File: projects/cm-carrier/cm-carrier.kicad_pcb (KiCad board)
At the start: 2 copper layers, 0 parts

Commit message: cm-carrier: PCB first pass (sync from schematic, 130x90 outline, block placement, DRC report)
Co-Authored-By: Claude Opus 5.5 <noreply@anthropic.com>
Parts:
- added C1: 10uF 25V, Capacitor_SMD:C_1210_3225Metric, F.Cu at (118.0, 121.0)
- added C10: 100nF, Capacitor_SMD:C_0402_1005Metric, F.Cu at (225.0, 157.0)
- added C11: 100nF, Capacitor_SMD:C_0402_1005Metric, F.Cu at (225.0, 160.0)
- added C12: 100nF, Capacitor_SMD:C_0402_1005Metric, F.Cu at (225.0, 163.0)
- added C13: 10uF 10V, Capacitor_SMD:C_0805_2012Metric, F.Cu at (211.0, 167.0)
- added C14: 10uF 10V, Capacitor_SMD:C_0805_2012Metric, F.Cu at (225.0, 167.0)
- added C15: 1uF 10V, Capacitor_SMD:C_0402_1005Metric, F.Cu at (213.0, 177.0)
- added C16: 1uF 10V, Capacitor_SMD:C_0402_1005Metric, F.Cu at (218.0, 177.0)
- added C17: 1uF 10V, Capacitor_SMD:C_0402_1005Metric, F.Cu at (223.0, 177.0)
- added C18: 10uF 10V, Capacitor_SMD:C_0805_2012Metric, F.Cu at (213.0, 180.5)
- added C19: 10uF 10V, Capacitor_SMD:C_0805_2012Metric, F.Cu at (218.0, 180.5)
- added C2: 100nF, Capacitor_SMD:C_0402_1005Metric, F.Cu at (121.0, 124.5)
- added C20: 10uF 10V, Capacitor_SMD:C_0805_2012Metric, F.Cu at (223.0, 180.5)
- added C21: 470uF, Capacitor_SMD:CP_Elec_8x10, F.Cu at (160.0, 158.0)
- added C22: 100nF, Capacitor_SMD:C_0402_1005Metric, F.Cu at (168.0, 155.0)
- added C23: 33pF, Capacitor_SMD:C_0402_1005Metric, F.Cu at (168.0, 157.5)
- added C24: 10pF, Capacitor_SMD:C_0402_1005Metric, F.Cu at (168.0, 160.0)
- added C25: 100nF, Capacitor_SMD:C_0402_1005Metric, F.Cu at (190.0, 154.0)
- added C26: 33pF, Capacitor_SMD:C_0402_1005Metric, F.Cu at (186.5, 159.0)
- added C27: 33pF, Capacitor_SMD:C_0402_1005Metric, F.Cu at (186.5, 161.5)
- added C28: 33pF, Capacitor_SMD:C_0402_1005Metric, F.Cu at (186.5, 164.0)
- added C29: 100nF, Capacitor_SMD:C_0402_1005Metric, F.Cu at (150.0, 180.0)
- added C3: 3.3nF, Capacitor_SMD:C_0402_1005Metric, F.Cu at (125.0, 125.0)
- added C30: 100nF, Capacitor_SMD:C_0402_1005Metric, F.Cu at (190.0, 175.5)
- added C31: 10uF, Capacitor_SMD:C_0805_2012Metric, F.Cu at (135.0, 116.0)
- added C4: 22uF 6.3V, Capacitor_SMD:C_0805_2012Metric, F.Cu at (137.0, 121.0)
- added C5: 27pF, Capacitor_SMD:C_0402_1005Metric, F.Cu at (213.5, 150.0)
- added C6: 27pF, Capacitor_SMD:C_0402_1005Metric, F.Cu at (222.5, 150.0)
- added C7: 100nF, Capacitor_SMD:C_0402_1005Metric, F.Cu at (211.0, 157.0)
- added C8: 100nF, Capacitor_SMD:C_0402_1005Metric, F.Cu at (211.0, 160.0)
- added C9: 100nF, Capacitor_SMD:C_0402_1005Metric, F.Cu at (211.0, 163.0)
- added D1: LED_ACT green, LED_SMD:LED_0603_1608Metric, F.Cu at (123.0, 113.0)
- added D2: green, LED_SMD:LED_0603_1608Metric, F.Cu at (183.0, 162.0)
- added H1: MountingHole_3.2mm_M3, MountingHole:MountingHole_3.2mm_M3, F.Cu at (104.0, 104.0)
- added H2: MountingHole_3.2mm_M3, MountingHole:MountingHole_3.2mm_M3, F.Cu at (226.0, 104.0)
- added H3: MountingHole_3.2mm_M3, MountingHole:MountingHole_3.2mm_M3, F.Cu at (104.0, 186.0)
- added H4: MountingHole_3.2mm_M3, MountingHole:MountingHole_3.2mm_M3, F.Cu at (226.0, 186.0)
- added J1: XA_5V_IN, Connector_JST:JST_XA_B08B-XASK-1_1x08_P2.50mm_Vertical, F.Cu at (111.0, 105.0)
- added J2: DEBUG_UART, Connector_PinHeader_2.54mm:PinHeader_1x03_P2.54mm_Vertical, F.Cu at (108.0, 112.0)
- added J3: USB_C_HOST (USB2.0), Connector_USB:USB_C_Receptacle_GCT_USB4105-xx-A_16P_TopMnt_Horizontal, F.Cu at (198.0, 186.3)
- added J4: XA_USB1, Connector_JST:JST_XA_B04B-XASK-1_1x04_P2.50mm_Vertical, F.Cu at (162.0, 105.0)
- added J5: XA_USB2, Connector_JST:JST_XA_B04B-XASK-1_1x04_P2.50mm_Vertical, F.Cu at (177.0, 105.0)
- added J6: EC25-J Mini PCIe, Connector_PCBEdge:BUS_PCI_Express_Mini_Full, F.Cu at (160.0, 135.0)
- added J7: nanoSIM, Connector_Card:nanoSIM_GCT_SIM8060-6-0-14-00, F.Cu at (200.0, 160.0)
- added J8: micro HDMI (Type D), Connector_Video:HDMI_Micro-D_Molex_46765-2xxx, F.Cu at (182.0, 187.6)
- added J9: microSD, Connector_Card:microSD_HC_Hirose_DM3AT-SF-PEJM5, F.Cu at (148.0, 108.9)
- added L1: 2.2uH XFL4020-222MEB, Inductor_SMD:L_Coilcraft_XxL4020, F.Cu at (131.0, 121.0)
- added Module1: CM4/CM5 (Lite), CM5IO:Raspberry-Pi-5-Compute-Module, F.Cu at (110.0, 178.0)
- added Q1: 2N7002, Package_TO_SOT_SMD:SOT-23, F.Cu at (173.0, 156.0)
- added Q2: 2N7002, Package_TO_SOT_SMD:SOT-23, F.Cu at (173.0, 162.0)
- added R1: 100k, Resistor_SMD:R_0402_1005Metric, F.Cu at (121.0, 118.5)
- added R10: 56k, Resistor_SMD:R_0402_1005Metric, F.Cu at (208.0, 178.0)
- added R11: 10k, Resistor_SMD:R_0402_1005Metric, F.Cu at (214.0, 141.5)
- added R12: 10k, Resistor_SMD:R_0402_1005Metric, F.Cu at (217.0, 141.5)
- added R13: 10k, Resistor_SMD:R_0402_1005Metric, F.Cu at (220.0, 141.5)
- added R14: 100k, Resistor_SMD:R_0402_1005Metric, F.Cu at (177.0, 156.0)
- added R15: 100k, Resistor_SMD:R_0402_1005Metric, F.Cu at (177.0, 162.0)
- added R16: 10k, Resistor_SMD:R_0402_1005Metric, F.Cu at (180.0, 156.0)
- added R17: 1k, Resistor_SMD:R_0402_1005Metric, F.Cu at (180.0, 162.0)
- added R18: 15k, Resistor_SMD:R_0402_1005Metric, F.Cu at (190.0, 156.5)
- added R19: 0R, Resistor_SMD:R_0402_1005Metric, F.Cu at (190.0, 159.0)
- added R2: 100k, Resistor_SMD:R_0402_1005Metric, F.Cu at (129.0, 125.5)
- added R20: 0R, Resistor_SMD:R_0402_1005Metric, F.Cu at (190.0, 161.5)
- added R21: 0R, Resistor_SMD:R_0402_1005Metric, F.Cu at (190.0, 164.0)
- added R22: 470R, Resistor_SMD:R_0402_1005Metric, F.Cu at (149.0, 184.0)
- added R23: 470R, Resistor_SMD:R_0402_1005Metric, F.Cu at (151.5, 184.0)
- added R24: 10k 1%, Resistor_SMD:R_0402_1005Metric, F.Cu at (138.5, 116.0)
- added R3: 1k, Resistor_SMD:R_0402_1005Metric, F.Cu at (123.0, 115.5)
- added R4: 12k 1%, Resistor_SMD:R_0402_1005Metric, F.Cu at (214.0, 145.0)
- added R5: 36k 1%, Resistor_SMD:R_0402_1005Metric, F.Cu at (217.0, 145.0)
- added R6: 36k 1%, Resistor_SMD:R_0402_1005Metric, F.Cu at (220.0, 145.0)
- added R7: 36k 1%, Resistor_SMD:R_0402_1005Metric, F.Cu at (223.0, 145.0)
- added R8: 36k 1%, Resistor_SMD:R_0402_1005Metric, F.Cu at (226.0, 145.0)
- added R9: 56k, Resistor_SMD:R_0402_1005Metric, F.Cu at (205.0, 178.0)
- added SW1: PWR_BUT, Button_Switch_SMD:SW_SPST_TL3342, F.Cu at (116.0, 114.0)
- added U1: TPS62132, Package_DFN_QFN:VQFN-16-1EP_3x3mm_P0.5mm_EP1.68x1.68mm_ThermalVias, F.Cu at (125.0, 121.0)
- added U10: TPD4EUSB30, Package_SON:USON-10_2.5x1.0mm_P0.5mm, F.Cu at (150.0, 172.0)
- added U11: TPD4EUSB30, Package_SON:USON-10_2.5x1.0mm_P0.5mm, F.Cu at (150.0, 176.0)
- added U12: MagJack A70-112-331N126, CM5IO:TRJG0926HENL, F.Cu at (163.0, 179.1)
- added U13: TPD4EUSB30, Package_SON:USON-10_2.5x1.0mm_P0.5mm, F.Cu at (178.0, 176.0)
- added U14: TPD4EUSB30, Package_SON:USON-10_2.5x1.0mm_P0.5mm, F.Cu at (182.0, 176.0)
- added U15: TPD4EUSB30, Package_SON:USON-10_2.5x1.0mm_P0.5mm, F.Cu at (186.0, 176.0)
- added U16: RT9742SNGV, Package_TO_SOT_SMD:TSOT-23_HandSoldering, F.Cu at (190.0, 171.0)
- added U17: RT9742GGJ5, Package_TO_SOT_SMD:SOT-23-5, F.Cu at (136.0, 112.0)
- added U2: USB2514B-I/M2, Package_DFN_QFN:QFN-36-1EP_6x6mm_P0.5mm_EP3.7x3.7mm, F.Cu at (218.0, 160.0)
- added U3: TPS2051CDBV, Package_TO_SOT_SMD:SOT-23-5, F.Cu at (213.0, 173.0)
- added U4: TPS2051CDBV, Package_TO_SOT_SMD:SOT-23-5, F.Cu at (218.0, 173.0)
- added U5: TPS2051CDBV, Package_TO_SOT_SMD:SOT-23-5, F.Cu at (223.0, 173.0)
- added U6: USBLC6-2SC6, Package_TO_SOT_SMD:SOT-23-6, F.Cu at (198.0, 178.0)
- added U7: USBLC6-2SC6, Package_TO_SOT_SMD:SOT-23-6, F.Cu at (166.0, 112.0)
- added U8: USBLC6-2SC6, Package_TO_SOT_SMD:SOT-23-6, F.Cu at (181.0, 112.0)
- added U9: TPD4E05U06DQA, Package_SON:USON-10_2.5x1.0mm_P0.5mm, F.Cu at (186.5, 155.0)
- added Y1: 24MHz CL=18pF, Crystal:Crystal_SMD_3225-4Pin_3.2x2.5mm, F.Cu at (218.0, 150.0)
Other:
- board outline added: 130 x 90 mm

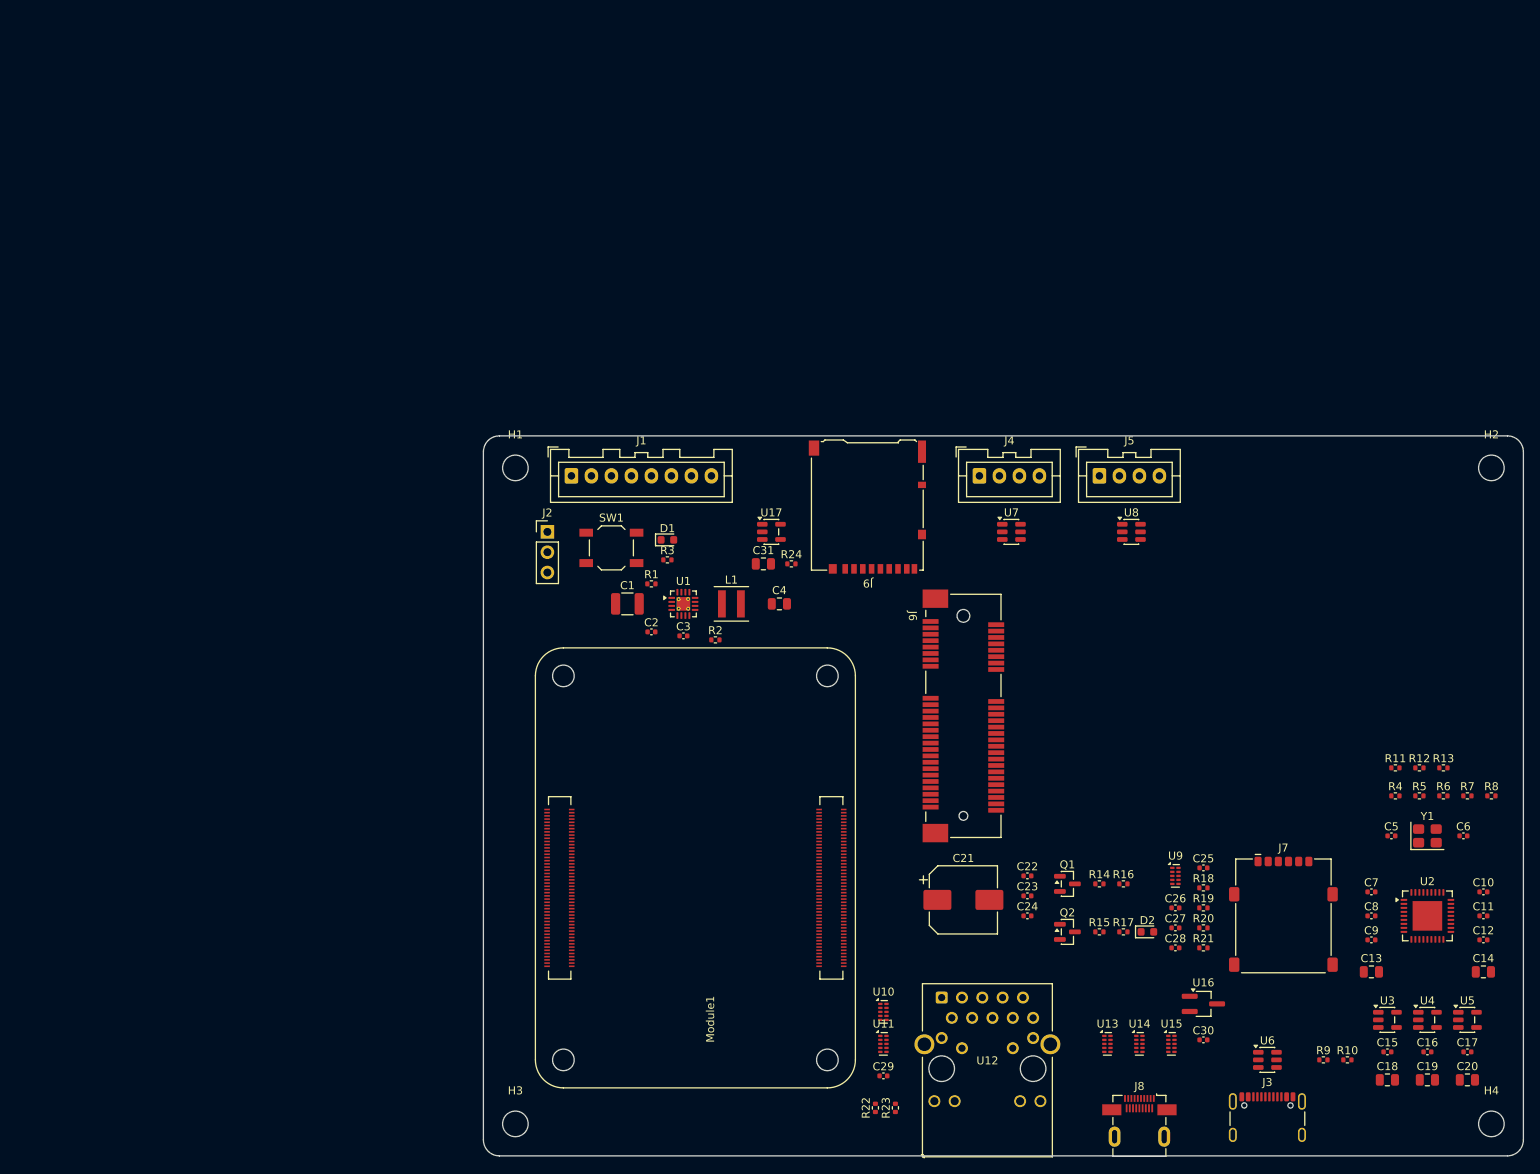
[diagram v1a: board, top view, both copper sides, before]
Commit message: cm-carrier: snapshot GUI-saved board before re-applying JLCPCB rules
Co-Authored-By: Claude Opus 5.5 <noreply@anthropic.com>
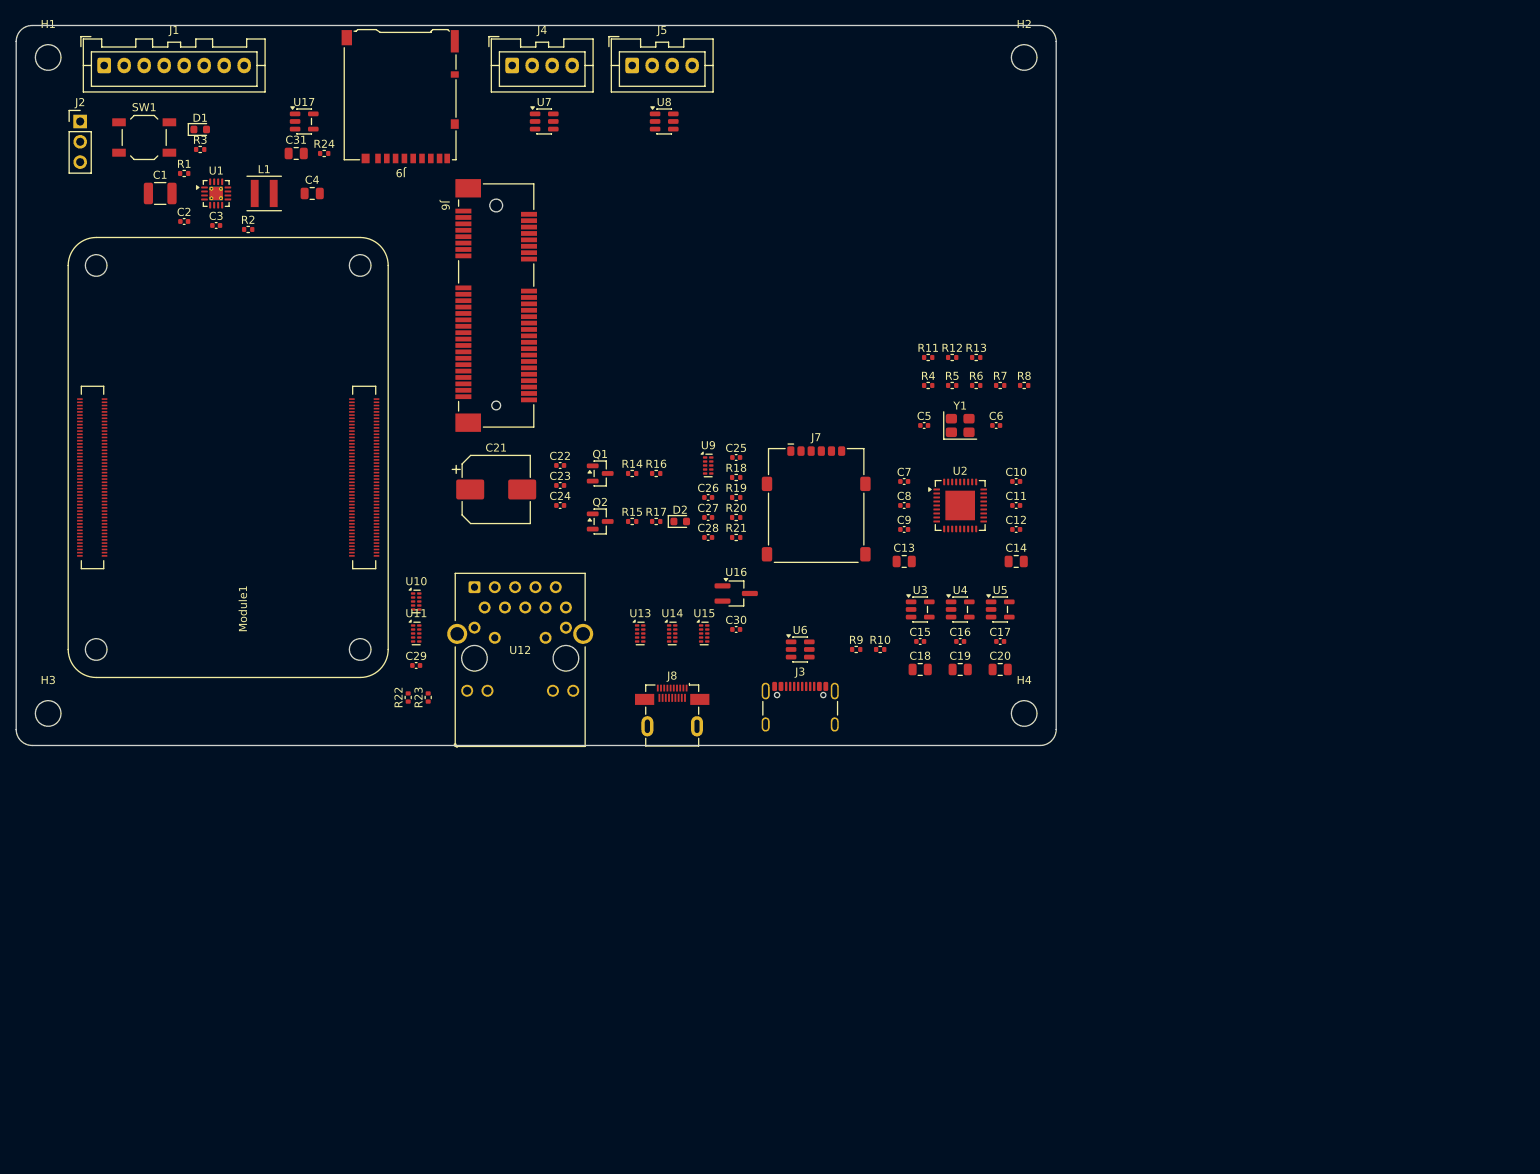
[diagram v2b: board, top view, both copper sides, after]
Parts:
- moved C18 77.7 mm to (154.6, 129.2)
- moved C19 77.7 mm to (159.6, 129.2)
- moved C20 77.7 mm to (164.6, 129.2)
- moved C29 77.7 mm to (91.6, 128.7)
- moved H4 77.7 mm to (167.6, 134.7)
- moved J3 77.7 mm to (139.6, 135.0)
- moved R22 77.7 mm to (90.6, 132.7)
- moved R23 77.7 mm to (93.1, 132.7)
- moved C10 77.7 mm to (166.6, 105.7)
- moved C11 77.7 mm to (166.6, 108.7)
- moved C12 77.7 mm to (166.6, 111.7)
- moved C13 77.7 mm to (152.6, 115.7)
- moved C14 77.7 mm to (166.6, 115.7)
- moved C15 77.7 mm to (154.6, 125.7)
- moved C16 77.7 mm to (159.6, 125.7)
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
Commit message: cm-carrier: 2-layer trial zones (B.Cu GND, F.Cu +5V strip); Freerouting plateaued at ~110/199 unrouted
Co-Authored-By: Claude Opus 5.5 <noreply@anthropic.com>
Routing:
- added copper zone on F.Cu, net +5V
- added copper zone on B.Cu, net GND
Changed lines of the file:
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@@
 		(layer "Edge.Cuts")
+	)
+	(zone
+		(net "+5V")
+		(layer "F.Cu")
+		(name "P5V_F")
+		(hatch edge 0.508)
+		(priority 1)
+		(connect_pads
+			(clearance 0.2)
+		)
+		(min_thickness 0.2)
+		(fill yes
+			(thermal_gap 0.5)
+			(thermal_bridge_width 0.5)
+			(island_removal_mode 0)
+		)
+		(polygon
+			(pts
+				(xy 42.1 49.2) (xy 63.5 49.2) (xy 63.5 66.5) (xy 70.5 66.5) (xy 70.5 76.5) (xy 51.5 76.5) (xy 51.5 114)
+				(xy 42.1 114)
+			)
+		)
+	)
+	(zone
+		(net "GND")
+		(layer "B.Cu")
+		(name "GND_B")
+		(hatch edge 0.508)
+		(connect_pads
+			(clearance 0.2)
+		)
+		(min_thickness 0.2)
+		(fill yes
+			(thermal_gap 0.5)
+			(thermal_bridge_width 0.5)
+			(island_removal_mode 0)
+		)
+		(polygon
+			(pts
+				(xy 42.1 49.2) (xy 171.1 49.2) (xy 171.1 138.2) (xy 42.1 138.2)
+			)
+		)
 	)
 	(embedded_fonts no)

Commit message: cm-carrier: go 4-layer (add In1.Cu/In2.Cu power layers), drop 2-layer trial zones
Co-Authored-By: Claude Opus 5.5 <noreply@anthropic.com>
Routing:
- removed copper zone on F.Cu, net +5V
- removed copper zone on B.Cu, net GND
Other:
- copper layers 2 -> 4
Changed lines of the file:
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@@
 		(35 "F.Fab" user)
 		(33 "B.Fab" user)
+		(4 "In1.Cu" power)
+		(6 "In2.Cu" power)
 	)
 	(setup
@@
 		(layer "Edge.Cuts")
 	)
-	(zone
-		(net "+5V")
-		(layer "F.Cu")
-		(name "P5V_F")
-		(hatch edge 0.508)
-		(priority 1)
-		(connect_pads
-			(clearance 0.2)
-		)
-		(min_thickness 0.2)
-		(fill yes
-			(thermal_gap 0.5)
-			(thermal_bridge_width 0.5)
-			(island_removal_mode 0)
-		)
-		(polygon
-			(pts
-				(xy 42.1 49.2) (xy 63.5 49.2) (xy 63.5 66.5) (xy 70.5 66.5) (xy 70.5 76.5) (xy 51.5 76.5) (xy 51.5 114)
-				(xy 42.1 114)
-			)
-		)
-	)
-	(zone
-		(net "GND")
-		(layer "B.Cu")
-		(name "GND_B")
-		(hatch edge 0.508)
-		(connect_pads
-			(clearance 0.2)
-		)
-		(min_thickness 0.2)
-		(fill yes
-			(thermal_gap 0.5)
-			(thermal_bridge_width 0.5)
-			(island_removal_mode 0)
-		)
-		(polygon
-			(pts
-				(xy 42.1 49.2) (xy 171.1 49.2) (xy 171.1 138.2) (xy 42.1 138.2)
-			)
-		)
-	)
 	(embedded_fonts no)

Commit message: cm-carrier: 4-layer planes (In1 GND, In2 +5V with +3V3_LTE island)
Co-Authored-By: Claude Opus 5.5 <noreply@anthropic.com>
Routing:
- added copper zone on In2.Cu, net +3V3_LTE
- added copper zone on In2.Cu, net +5V
- added copper zone on In1.Cu, net GND
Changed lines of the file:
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@@
 	(layers
 		(0 "F.Cu" signal)
+		(4 "In1.Cu" power)
+		(6 "In2.Cu" power)
 		(2 "B.Cu" signal)
 		(9 "F.Adhes" user "F.Adhesive")
@@
 		(35 "F.Fab" user)
 		(33 "B.Fab" user)
-		(4 "In1.Cu" power)
-		(6 "In2.Cu" power)
 	)
 	(setup
@@
 		(layer "Edge.Cuts")
 	)
+	(zone
+		(net "GND")
+		(layer "In1.Cu")
+		(name "GND_In1")
+		(hatch edge 0.508)
+		(connect_pads
+			(clearance 0.2)
+		)
+		(min_thickness 0.2)
+		(fill yes
+			(thermal_gap 0.5)
+			(thermal_bridge_width 0.5)
+			(island_removal_mode 0)
+		)
+		(polygon
+			(pts
+				(xy 42.1 49.2) (xy 171.1 49.2) (xy 171.1 138.2) (xy 42.1 138.2)
+			)
+		)
+	)
+	(zone
+		(net "+5V")
+		(layer "In2.Cu")
+		(name "P5V_In2")
+		(hatch edge 0.508)
+		(connect_pads
+			(clearance 0.2)
+		)
+		(min_thickness 0.2)
+		(fill yes
+			(thermal_gap 0.5)
+			(thermal_bridge_width 0.5)
+			(island_removal_mode 0)
+		)
+		(polygon
+			(pts
+				(xy 42.1 49.2) (xy 171.1 49.2) (xy 171.1 138.2) (xy 42.1 138.2)
+			)
+		)
+	)
+	(zone
+		(net "+3V3_LTE")
+		(layer "In2.Cu")
+		(name "P3V3LTE_In2")
+		(hatch edge 0.508)
+		(priority 1)
+		(connect_pads
+			(clearance 0.3)
+		)
+		(min_thickness 0.2)
+		(fill yes
+			(thermal_gap 0.5)
+			(thermal_bridge_width 0.5)
+			(island_removal_mode 0)
+		)
+		(polygon
+			(pts
+				(xy 70 66) (xy 112 66) (xy 112 112) (xy 70 112)
+			)
+		)
+	)
 	(embedded_fonts no)

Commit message: cm-carrier: import signal-only Freerouting result (plane nets excluded)
Co-Authored-By: Claude Opus 5.5 <noreply@anthropic.com>
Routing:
- net +3V3: track 0.00 -> 210.4 mm
- net HUB_RESET_N: track 0.00 -> 145.2 mm, vias 0 -> 2
- net /USB Hub/P3_VBUS: track 0.00 -> 114.4 mm, vias 0 -> 2
- net /USB Hub/P4_VBUS: track 0.00 -> 109.5 mm, vias 0 -> 1
- net ETH_P2_N: track 0.00 -> 108.8 mm, vias 0 -> 1
- net /USB Hub/P3_DP: track 0.00 -> 100.4 mm, vias 0 -> 1
- net ETH_P3_N: track 0.00 -> 98.6 mm
- net ETH_P2_P: track 0.00 -> 96.1 mm, vias 0 -> 2
- net USB_HOST_N: track 0.00 -> 88.5 mm, vias 0 -> 2
- net ETH_P3_P: track 0.00 -> 88.3 mm
- net HDMI0_CEC: track 0.00 -> 87.2 mm
- net USB_HOST_P: track 0.00 -> 86.5 mm, vias 0 -> 2
- net /USB Hub/P4_DM: track 0.00 -> 84.0 mm, vias 0 -> 1
- net /USB Hub/P4_DP: track 0.00 -> 83.7 mm, vias 0 -> 1
- net LTE_AIRPLANE: track 0.00 -> 81.0 mm, vias 0 -> 2
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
